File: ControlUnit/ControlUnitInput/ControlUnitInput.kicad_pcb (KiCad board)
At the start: 2 copper layers, 100.1 x 90 mm, 43 parts, among them SW1 SW_Push, SW10 SW_Push, SW11 SW_Push, SW13 SW_Push, SW14 SW_Push, SW15 SW_Push, SW16 SW_Push, SW2 SW_Push, SW3 SW_Push, SW4 SW_Push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

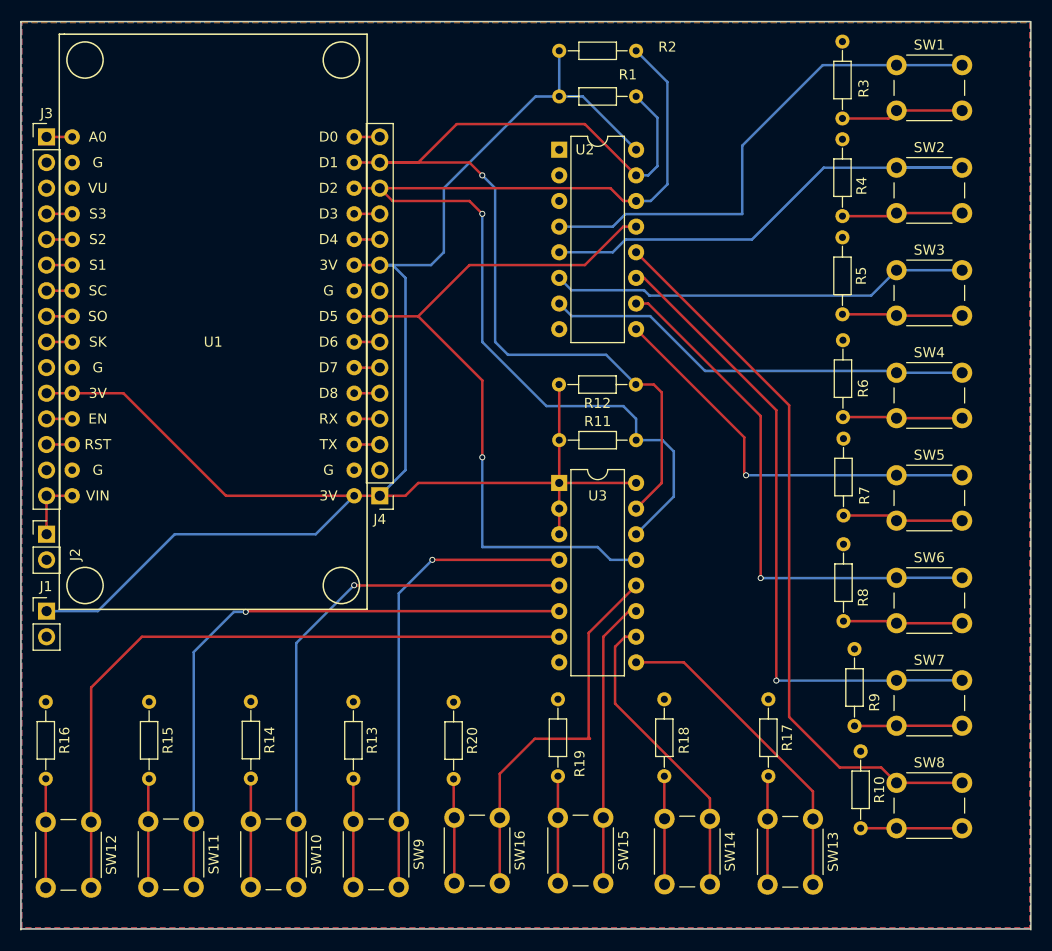
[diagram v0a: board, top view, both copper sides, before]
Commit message: 0.4 - 0.5 mm track thickness
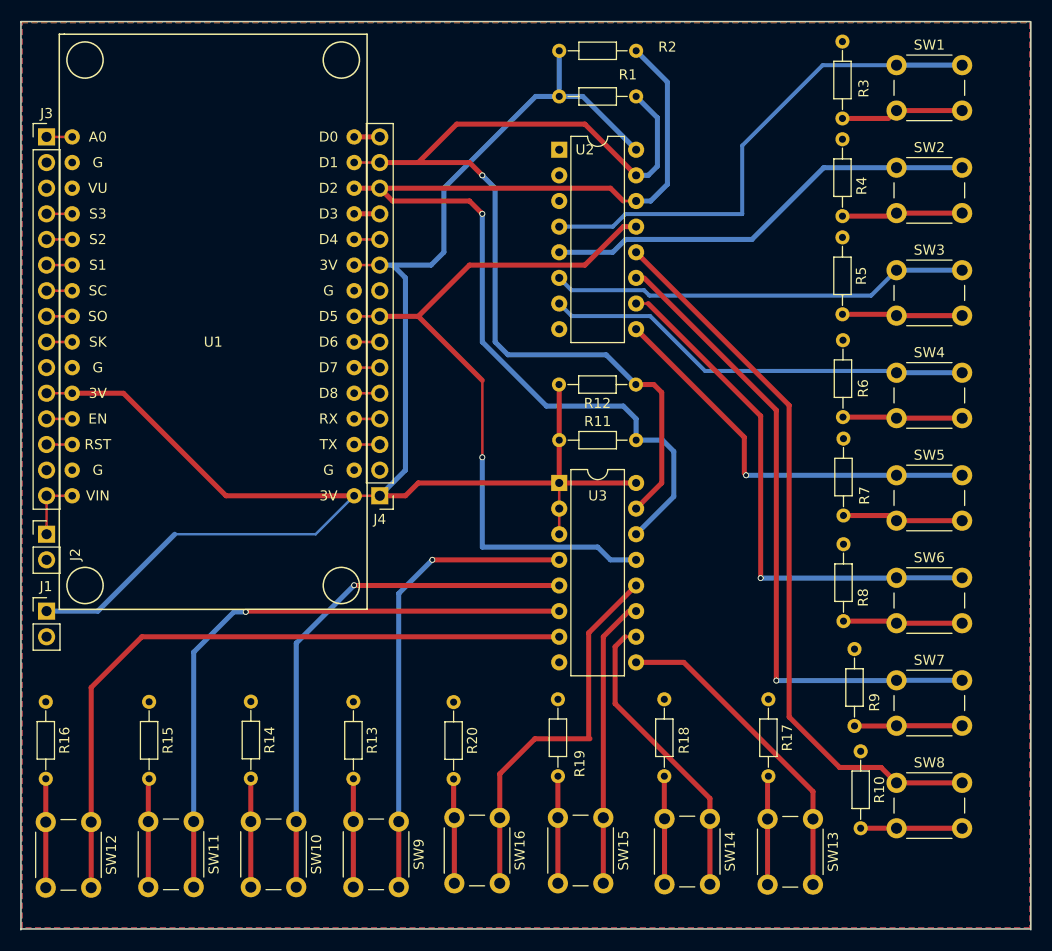
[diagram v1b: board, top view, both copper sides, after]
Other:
- net class Default: trace_width 0.25 -> 0.5

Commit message: prepared to order pcbs
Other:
- board size 100.1 x 90 mm -> 96.1 x 90.1 mm
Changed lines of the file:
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@@
     (visible_elements 7FFFFFFF)
     (pcbplotparams
-      (layerselection 0x00030_80000001)
+      (layerselection 0x010f0_80000001)
       (usegerberextensions false)
+      (usegerberattributes true)
       (excludeedgelayer true)
       (linewidth 0.100000)
@@
       (outputformat 1)
       (mirror false)
-      (drillshape 1)
+      (drillshape 0)
       (scaleselection 1)
-      (outputdirectory ""))
+      (outputdirectory Gerbers/))
   )
   (net 0 "")
@@
     (effects (font (size 1.5 1.5) (thickness 0.3)))
   )
-  (gr_text "Rev  0.2" (at 106.0704 99.8728) (layer Eco2.User)
+  (gr_text "Rev  0.2" (at 55.88 17.78) (layer Eco2.User)
     (effects (font (size 1.5 1.5) (thickness 0.3)))
   )
-  (gr_text "Board design by Keroth & CodingSpiderFox\nLicense: CERN OHL v1.2" (at 109.601 46.863 90) (layer F.Fab)
+  (gr_text "Board design by Keroth & CodingSpiderFox\nLicense: CERN OHL v1.2" (at 33.02 36.83 90) (layer F.Fab)
     (effects (font (size 1.016 1.016) (thickness 0.254)))
   )
-  (gr_line (start 112.776 12.7) (end 112.776 102.7) (angle 90) (layer Edge.Cuts) (width 0.15))
-  (gr_line (start 12.7 12.7) (end 112.7 12.7) (angle 90) (layer Edge.Cuts) (width 0.15))
-  (gr_line (start 12.7 102.616) (end 112.7 102.616) (angle 90) (layer Edge.Cuts) (width 0.15))
+  (gr_line (start 108.7882 12.6365) (end 108.7882 102.6365) (angle 90) (layer Edge.Cuts) (width 0.15))
+  (gr_line (start 12.7 12.7) (end 108.7 12.7) (angle 90) (layer Edge.Cuts) (width 0.15))
+  (gr_line (start 12.7 102.616) (end 108.7 102.616) (angle 90) (layer Edge.Cuts) (width 0.15))
   (gr_line (start 12.7 12.7) (end 12.7 102.7) (angle 90) (layer Edge.Cuts) (width 0.15))
   (segment (start 15.24 24.13) (end 17.78 24.13) (width 0.25) (layer F.Cu) (net 1))
